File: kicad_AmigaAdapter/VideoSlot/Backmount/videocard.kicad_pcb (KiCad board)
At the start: 2 copper layers, 91.8 x 74.5 mm, 14 parts, among them J1 A2000_Video_Slot_Phys, U1 74LVC86, U2 74LVC574, U3 74LVC574

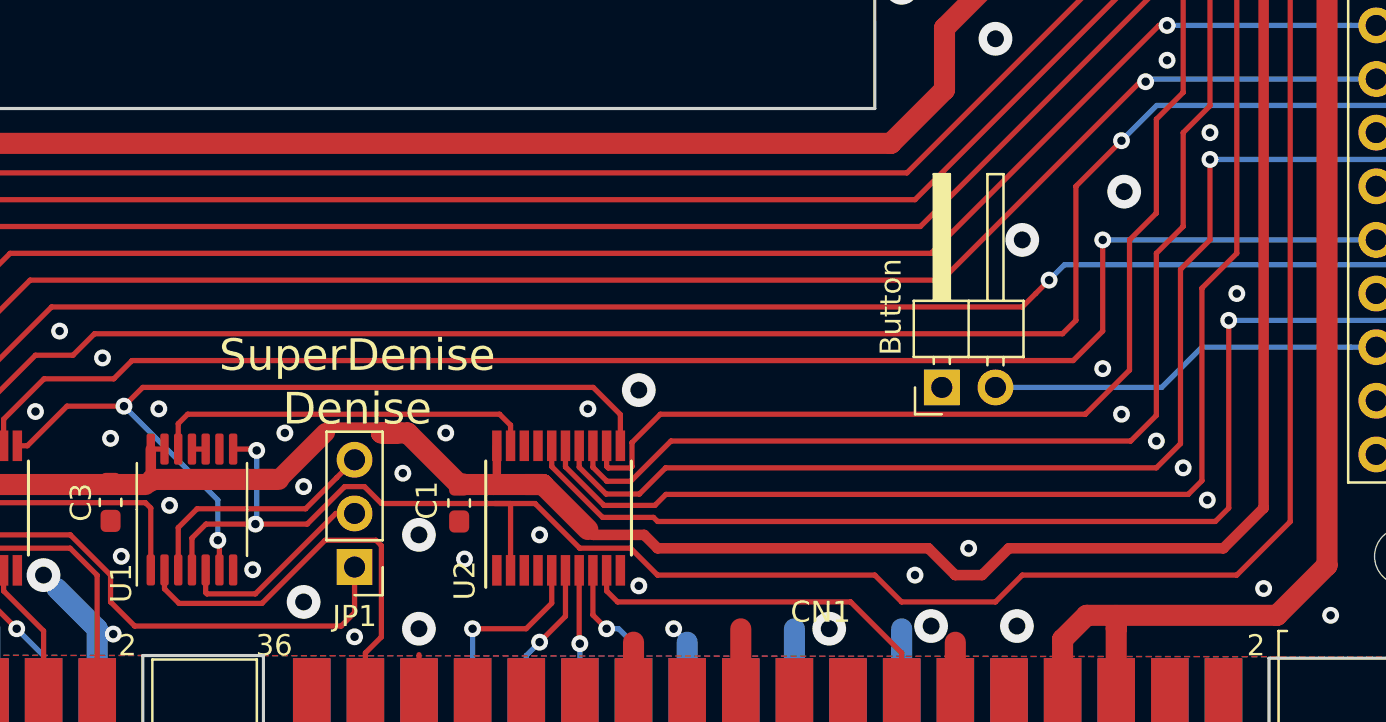
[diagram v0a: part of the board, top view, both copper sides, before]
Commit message: Edit Silk Screen for A2000 Backmount
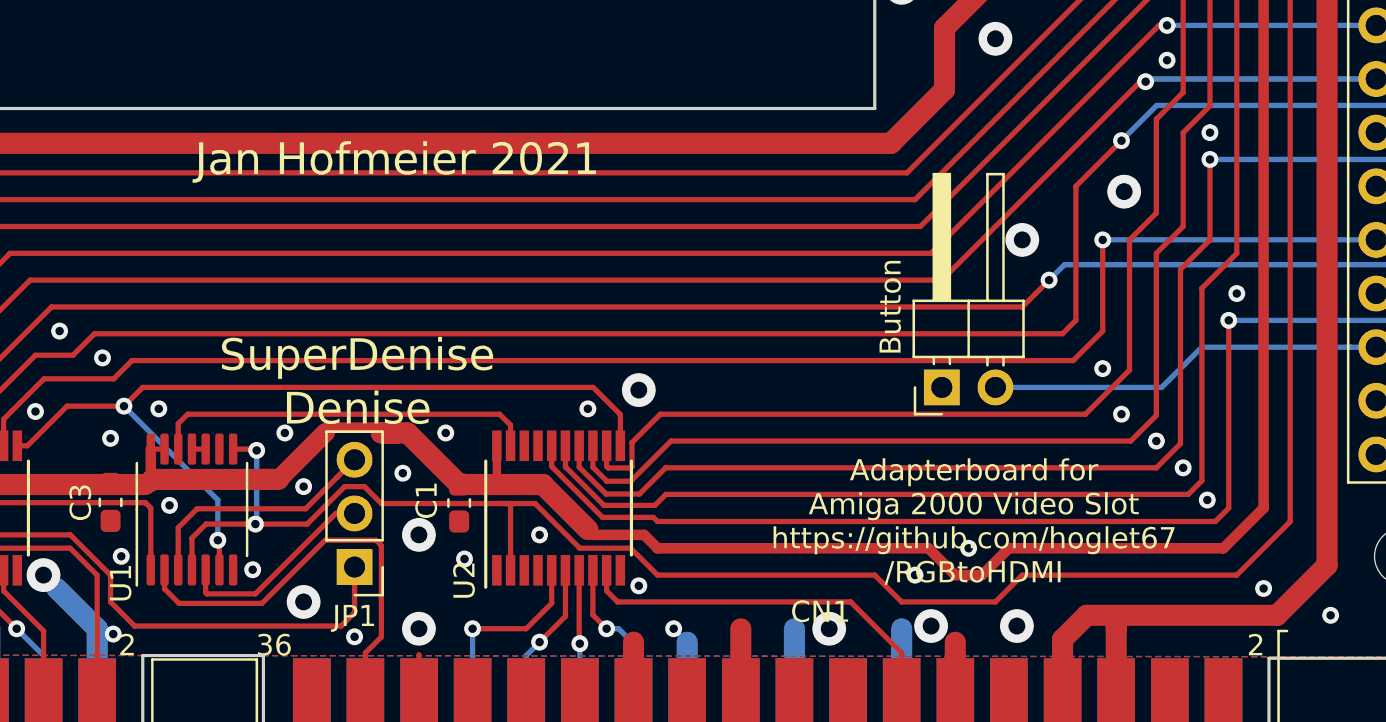
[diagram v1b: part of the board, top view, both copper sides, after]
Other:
- board text added: "Adapterboard for Amiga 2000 Video Slot https://github.com/hoglet67 /RGBtoHDMI"
- board text added: "Jan Hofmeier 2021"
- board text removed: "Adapterboard for Amiga Rev.2 https://github.com/hoglet67 /RGBtoHDMI"
